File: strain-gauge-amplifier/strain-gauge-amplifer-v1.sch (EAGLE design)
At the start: 19 parts, among them IC2 INA125U, Q1 PMV45EN

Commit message: Cleaned up schematic, fixed a minor errors, ready for layout!
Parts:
- removed JP4: POT, SparkFun-Connectors:M025MM
- removed R2: 120, rcl_custom:R-US_0805-C-NOSILK
- removed R9: POT, SparkFun-Electromechanical:TRIMPOTTRIMPOT-5MM
- added C2, C4: 100n, rcl_custom:C-EU0805-C-NOSILK
- added C5: 1n, rcl_custom:C-EU0805-C-NOSILK
- added R2A: 100, rcl_custom:R-US_0805-C-NOSILK
- added R2B: 50ohm/20turn, SparkFun-Electromechanical:TRIMPOTTRIMPOT-5MM
- JP2: value OUT1 -> (none)
- JP3: value OUT2 -> (none)
- JP5: value RGAIN -> Rg
- R10: value 150 -> 1k
- R3: value 100 -> 120
- R4: value 100 -> 1k
- R6: value 0 -> NP (0)
- R7: value DNP/10k -> NP (10k)
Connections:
- removed net N$7: R3.1, R9.CCW
- net 2.5VREF: now also C2.1, C4.1, C5.1, JP1.2, R1.2; no longer JP4.2
- net GND: now also C2.2, C4.2, C5.2, R2B.CW, R3.1; no longer R2.1, R9.CW
- net N$1: now also R2A.1, R2B.WIPER; no longer JP1.2, JP4.1, R1.2
- net VIN+: now also R2A.2; no longer R3.2
- net VIN-: now also R3.2; no longer R2.2
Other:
- note added: "To DAQ"
- note removed: "50 OHM/20 TURNS"
- moved on the sheet: C1, C3, IC2, JP1, JP2, JP3, JP5, LED1, Q1, R1, R10, R3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

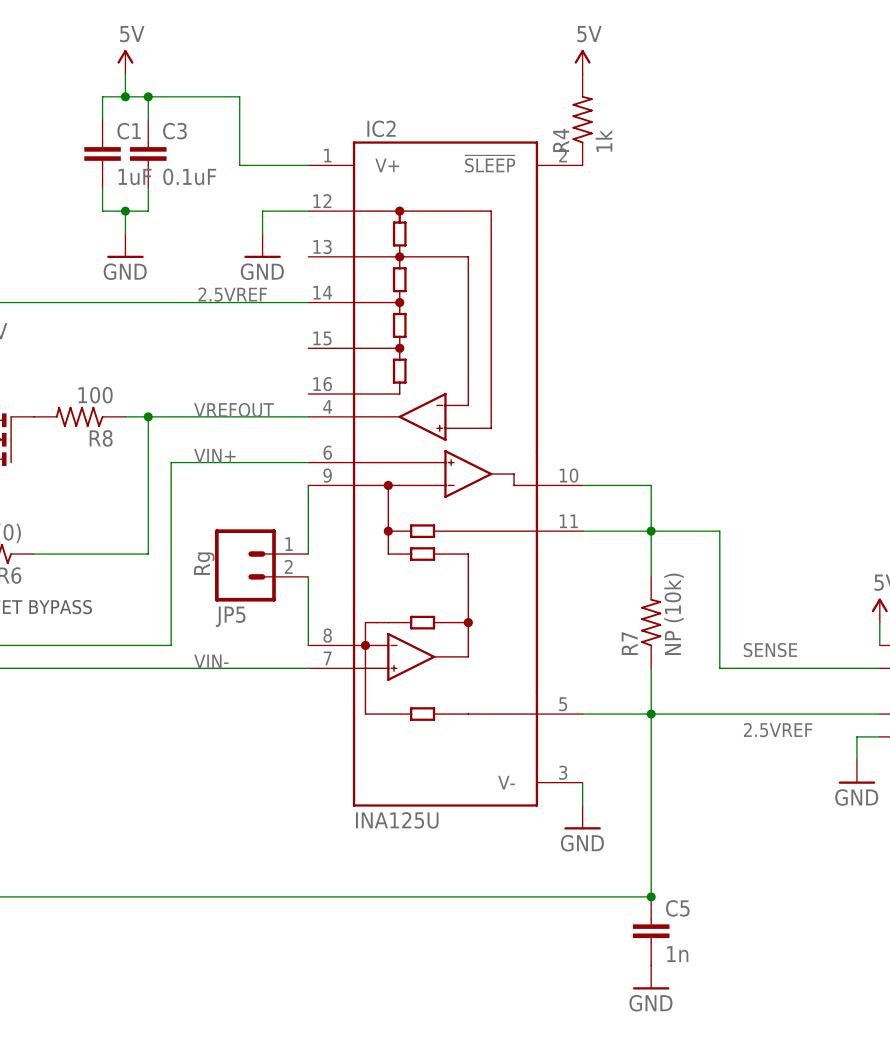
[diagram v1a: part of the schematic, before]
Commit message: Cleaned up and added BOM.
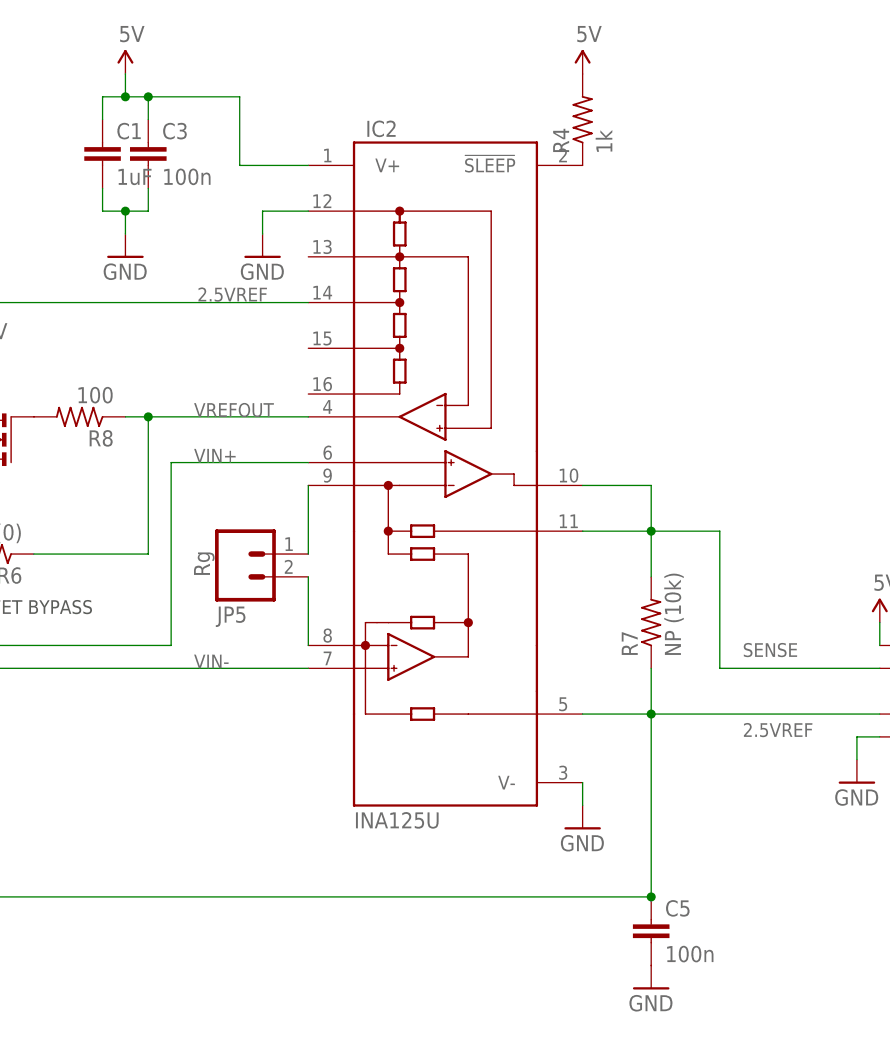
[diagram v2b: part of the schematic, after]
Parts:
- C3: value 0.1uF -> 100n
- C5: value 1n -> 100n
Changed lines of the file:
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@@
 <setting verticaltext="up"/>
 </settings>
-<grid distance="0.05" unitdist="inch" unit="inch" style="lines" multiple="2" display="yes" altdistance="0.01" altunitdist="inch" altunit="inch"/>
+<grid distance="0.1" unitdist="inch" unit="inch" style="lines" multiple="1" display="no" altdistance="0.01" altunitdist="inch" altunit="inch"/>
 <layers>
 <layer number="1" name="Top" color="4" fill="1" visible="no" active="no"/>
@@
 <parts>
 <part name="R4" library="rcl_custom" deviceset="R-US_" device="0805-C-NOSILK" value="1k"/>
-<part name="C3" library="rcl_custom" deviceset="C-EU" device="0805-C-NOSILK" value="0.1uF"/>
+<part name="C3" library="rcl_custom" deviceset="C-EU" device="0805-C-NOSILK" value="100n"/>
 <part name="U$3" library="SparkFun-Aesthetics" deviceset="5V" device=""/>
 <part name="JP1" library="SparkFun-Connectors" deviceset="M02" device="5MM" value="STRAIN"/>
@@
 <part name="C4" library="rcl_custom" deviceset="C-EU" device="0805-C-NOSILK" value="100n"/>
 <part name="GND8" library="SparkFun-Aesthetics" deviceset="GND" device=""/>
-<part name="C5" library="rcl_custom" deviceset="C-EU" device="0805-C-NOSILK" value="1n"/>
+<part name="C5" library="rcl_custom" deviceset="C-EU" device="0805-C-NOSILK" value="100n"/>
 <part name="GND9" library="SparkFun-Aesthetics" deviceset="GND" device=""/>
 </parts>
@@
 </sheet>
 </sheets>
+<errors>
+</errors>
 </schematic>
 </drawing>

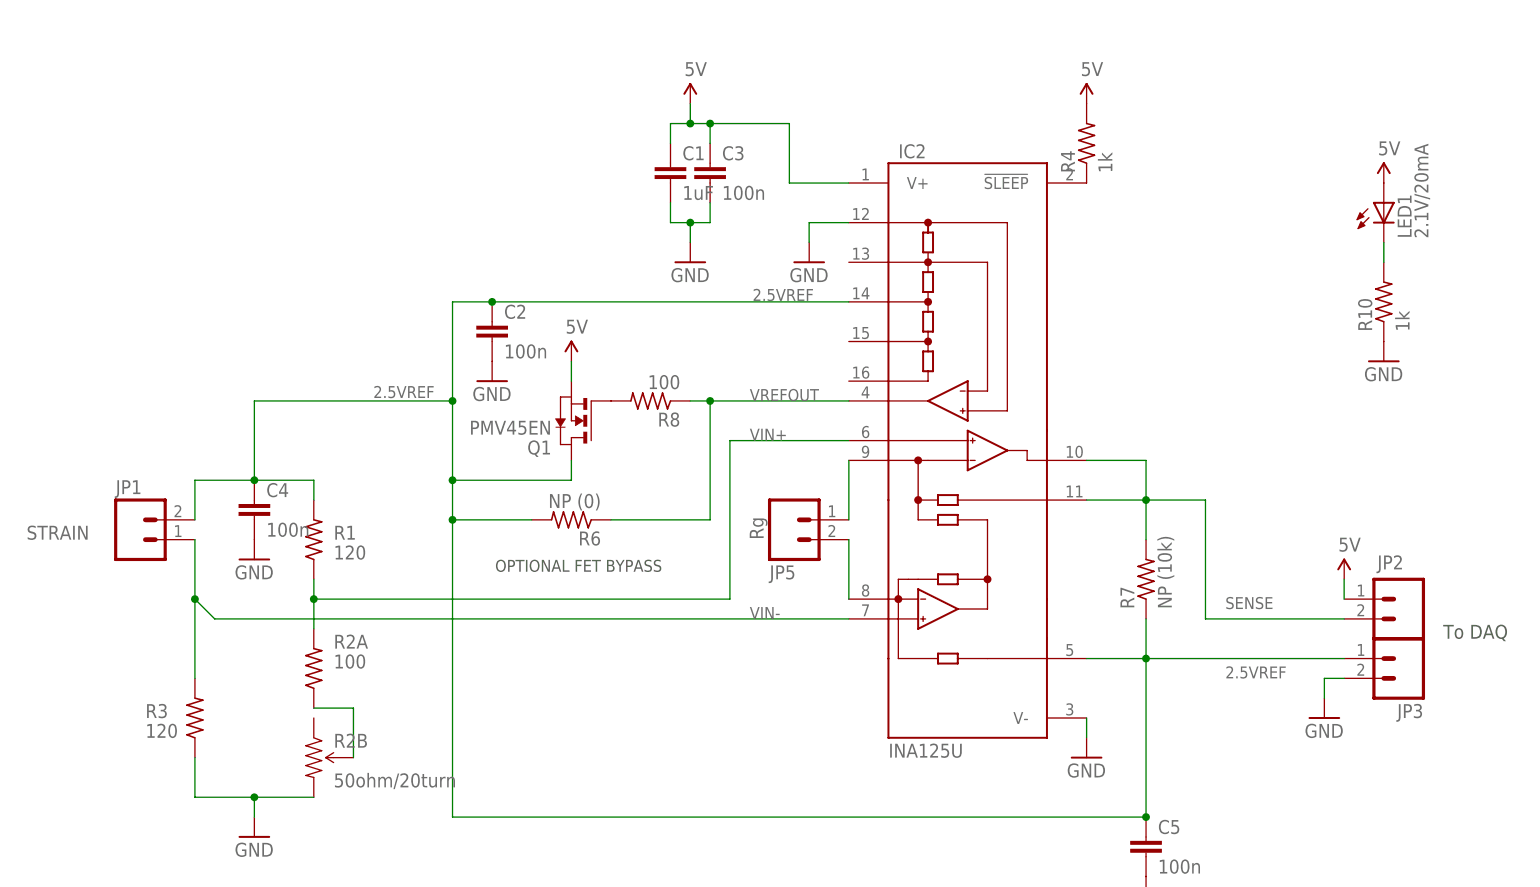
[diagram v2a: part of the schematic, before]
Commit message: Made board. Passes ERC, DRC.
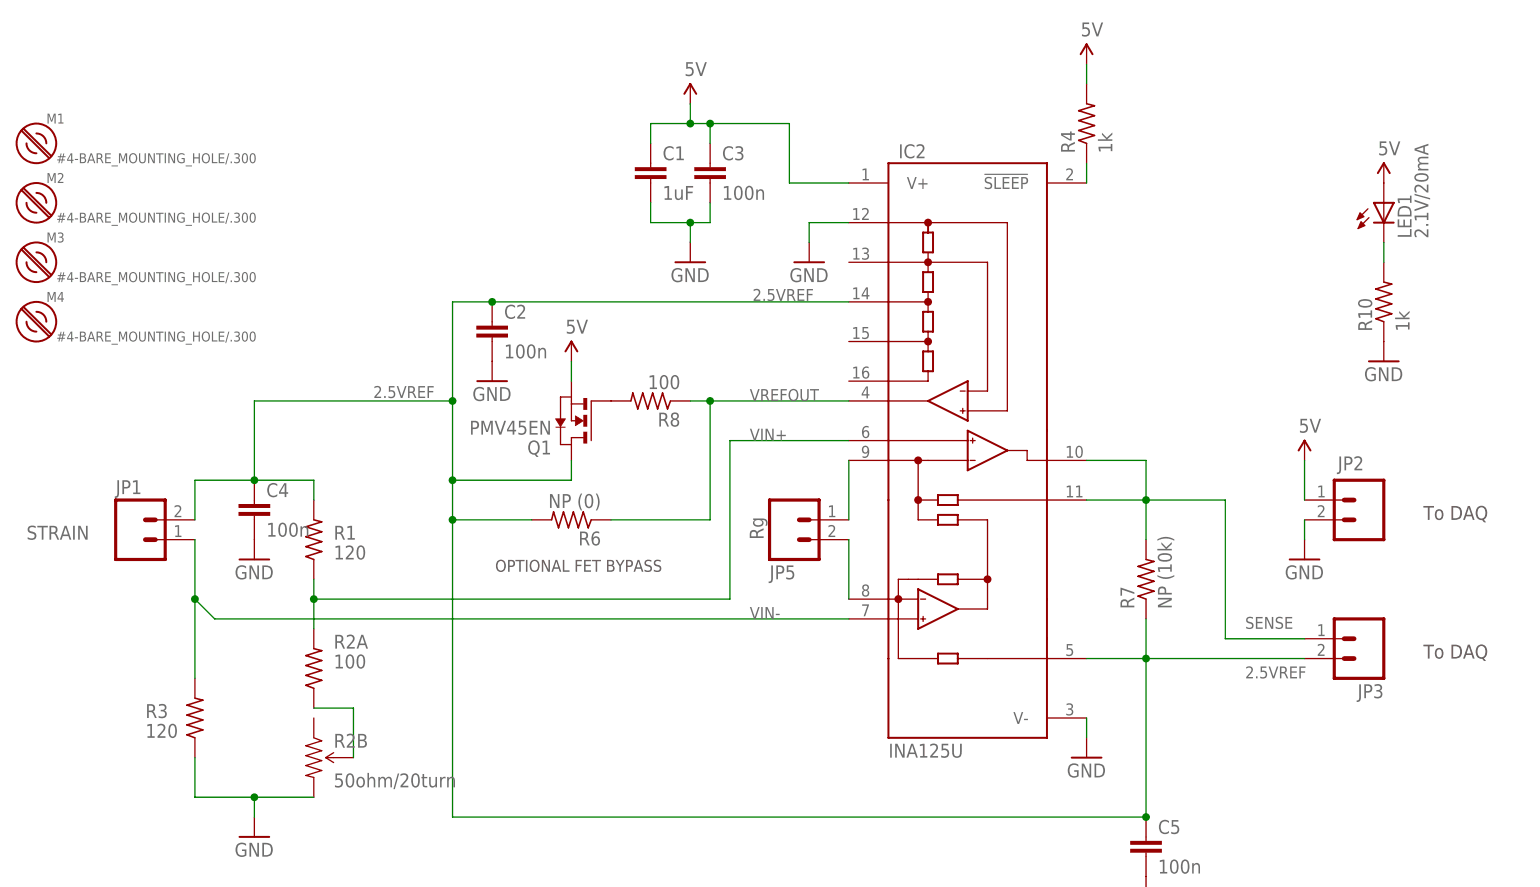
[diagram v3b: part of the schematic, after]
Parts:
- added M1, M2, M3, M4: #4-BARE_MOUNTING_HOLE/.300, mount:#4-BARE_MOUNTING_HOLE/.300
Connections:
- net 2.5VREF: now also JP3.2; no longer JP3.1
- net GND: now also JP2.2; no longer JP3.2
- net SENSE: now also JP3.1; no longer JP2.2
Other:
- moved on the sheet: C1, JP2, JP3, R4
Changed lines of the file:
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@@
 <?xml version="1.0" encoding="utf-8"?>
 <!DOCTYPE eagle SYSTEM "eagle.dtd">
-<eagle version="6.5.0">
+<eagle version="6.4">
 <drawing>
 <settings>
@@
 <setting verticaltext="up"/>
 </settings>
-<grid distance="0.1" unitdist="inch" unit="inch" style="lines" multiple="1" display="no" altdistance="0.01" altunitdist="inch" altunit="inch"/>
+<grid distance="0.1" unitdist="inch" unit="inch" style="dots" multiple="1" display="yes" altdistance="0.001" altunitdist="inch" altunit="inch"/>
 <layers>
 <layer number="1" name="Top" color="4" fill="1" visible="no" active="no"/>
@@
 <part name="C5" library="rcl_custom" deviceset="C-EU" device="0805-C-NOSILK" value="100n"/>
 <part name="GND9" library="SparkFun-Aesthetics" deviceset="GND" device=""/>
+<part name="M1" library="mount" deviceset="#4-BARE_MOUNTING_HOLE" device="/.300"/>
+<part name="M2" library="mount" deviceset="#4-BARE_MOUNTING_HOLE" device="/.300"/>
+<part name="M3" library="mount" deviceset="#4-BARE_MOUNTING_HOLE" device="/.300"/>
+<part name="M4" library="mount" deviceset="#4-BARE_MOUNTING_HOLE" device="/.300"/>
 </parts>
 <sheets>
@@
 <plain>
 <text x="94.361" y="107.6452" size="1.524" layer="97">OPTIONAL FET BYPASS</text>
-<text x="215.9" y="99.06" size="1.778" layer="97">To DAQ</text>
+<text x="213.36" y="96.52" size="1.778" layer="97">To DAQ</text>
+<text x="213.36" y="114.3" size="1.778" layer="97">To DAQ</text>
 </plain>
 <instances>
-<instance part="R4" gate="R" x="170.18" y="162.56" rot="R90"/>
+<instance part="R4" gate="R" x="170.18" y="165.1" rot="R90"/>
 <instance part="C3" gate="CE" x="121.92" y="160.02"/>
 <instance part="U$3" gate="G$1" x="119.38" y="167.64"/>
@@
 <attribute name="NAME" x="45.72" y="117.602" size="1.778" layer="95"/>
 </instance>
-<instance part="JP2" gate="G$1" x="210.82" y="104.14" smashed="yes" rot="R180">
-<attribute name="VALUE" x="213.36" y="109.22" size="1.778" layer="96" rot="R180"/>
-<attribute name="NAME" x="210.82" y="109.728" size="1.778" layer="95" rot="R180"/>
-</instance>
-<instance part="JP3" gate="G$1" x="210.82" y="96.52" rot="R180"/>
+<instance part="JP2" gate="G$1" x="205.74" y="116.84" smashed="yes" rot="R180">
+<attribute name="VALUE" x="208.28" y="121.92" size="1.778" layer="96" rot="R180"/>
+<attribute name="NAME" x="205.74" y="122.428" size="1.778" layer="95" rot="R180"/>
+</instance>
+<instance part="JP3" gate="G$1" x="205.74" y="99.06" rot="R180"/>
 <instance part="R3" gate="R" x="55.88" y="88.9" smashed="yes" rot="R90">
 <attribute name="NAME" x="49.53" y="88.9" size="1.778" layer="95"/>
@@
 </instance>
 <instance part="GND2" gate="1" x="119.38" y="147.32"/>
-<instance part="U$1" gate="G$1" x="170.18" y="167.64"/>
-<instance part="GND1" gate="1" x="200.66" y="88.9"/>
+<instance part="U$1" gate="G$1" x="170.18" y="172.72"/>
+<instance part="GND1" gate="1" x="198.12" y="109.22"/>
 <instance part="R7" gate="R" x="177.8" y="106.68" rot="R90"/>
 <instance part="Q1" gate="G$1" x="104.14" y="127" rot="R180"/>
@@
 <instance part="R10" gate="R" x="208.28" y="142.24" rot="R90"/>
 <instance part="GND3" gate="1" x="208.28" y="134.62"/>
-<instance part="C1" gate="CE" x="116.84" y="160.02"/>
+<instance part="C1" gate="CE" x="114.3" y="160.02"/>
 <instance part="JP5" gate="G$1" x="132.08" y="114.3" smashed="yes" rot="MR180">
 <attribute name="VALUE" x="127" y="111.76" size="1.778" layer="96" rot="MR90"/>
@@
 <instance part="FRAME1" gate="G$1" x="0" y="0"/>
 <instance part="FRAME1" gate="G$2" x="172.72" y="0"/>
-<instance part="U$4" gate="G$1" x="203.2" y="106.68"/>
+<instance part="U$4" gate="G$1" x="198.12" y="121.92"/>
 <instance part="GND4" gate="1" x="170.18" y="83.82"/>
 <instance part="U$5" gate="G$1" x="208.28" y="157.48"/>
@@
 <instance part="C5" gate="CE" x="177.8" y="73.66"/>
 <instance part="GND9" gate="1" x="177.8" y="66.04"/>
+<instance part="M1" gate="MT" x="35.56" y="162.56"/>
+<instance part="M2" gate="MT" x="35.56" y="154.94"/>
+<instance part="M3" gate="MT" x="35.56" y="147.32"/>
+<instance part="M4" gate="MT" x="35.56" y="139.7"/>
 </instances>
 <busses>
@@
 <wire x1="121.92" y1="152.4" x2="121.92" y2="154.94" width="0.1524" layer="91"/>
 <pinref part="C1" gate="CE" pin="2"/>
-<wire x1="116.84" y1="154.94" x2="116.84" y2="152.4" width="0.1524" layer="91"/>
-<wire x1="116.84" y1="152.4" x2="119.38" y2="152.4" width="0.1524" layer="91"/>
+<wire x1="114.3" y1="154.94" x2="114.3" y2="152.4" width="0.1524" layer="91"/>
+<wire x1="114.3" y1="152.4" x2="119.38" y2="152.4" width="0.1524" layer="91"/>
 <wire x1="119.38" y1="152.4" x2="121.92" y2="152.4" width="0.1524" layer="91"/>
 <wire x1="119.38" y1="149.86" x2="119.38" y2="152.4" width="0.1524" layer="91"/>
@@
 <pinref part="GND4" gate="1" pin="GND"/>
 <wire x1="170.18" y1="86.36" x2="170.18" y2="88.9" width="0.1524" layer="91"/>
-</segment>
-<segment>
-<pinref part="GND1" gate="1" pin="GND"/>
-<pinref part="JP3" gate="G$1" pin="2"/>
-<wire x1="203.2" y1="93.98" x2="200.66" y2="93.98" width="0.1524" layer="91"/>
-<wire x1="200.66" y1="93.98" x2="200.66" y2="91.44" width="0.1524" layer="91"/>
 </segment>
 <segment>
@@
 <pinref part="GND9" gate="1" pin="GND"/>
 </segment>
+<segment>
+<pinref part="JP2" gate="G$1" pin="2"/>
+<pinref part="GND1" gate="1" pin="GND"/>
+<wire x1="198.12" y1="111.76" x2="198.12" y2="114.3" width="0.1524" layer="91"/>
+</segment>
 </net>
 <net name="N$3" class="0">
@@
 <wire x1="177.8" y1="116.84" x2="170.18" y2="116.84" width="0.1524" layer="91"/>
 <junction x="177.8" y="116.84"/>
-<wire x1="177.8" y1="116.84" x2="185.42" y2="116.84" width="0.1524" layer="91"/>
-<wire x1="185.42" y1="116.84" x2="185.42" y2="101.6" width="0.1524" layer="91"/>
-<wire x1="185.42" y1="101.6" x2="203.2" y2="101.6" width="0.1524" layer="91"/>
-<label x="187.96" y="102.87" size="1.524" layer="95"/>
+<wire x1="177.8" y1="116.84" x2="187.96" y2="116.84" width="0.1524" layer="91"/>
+<wire x1="187.96" y1="116.84" x2="187.96" y2="99.06" width="0.1524" layer="91"/>
+<wire x1="187.96" y1="99.06" x2="198.12" y2="99.06" width="0.1524" layer="91"/>
+<label x="190.5" y="100.33" size="1.524" layer="95"/>
 <pinref part="R7" gate="R" pin="2"/>
 <wire x1="177.8" y1="116.84" x2="177.8" y2="111.76" width="0.1524" layer="91"/>
-<pinref part="JP2" gate="G$1" pin="2"/>
+<pinref part="JP3" gate="G$1" pin="1"/>
 </segment>
 </net>
@@
 <wire x1="121.92" y1="165.1" x2="119.38" y2="165.1" width="0.1524" layer="91"/>
 <pinref part="C1" gate="CE" pin="1"/>
-<wire x1="119.38" y1="165.1" x2="116.84" y2="165.1" width="0.1524" layer="91"/>
-<wire x1="116.84" y1="165.1" x2="116.84" y2="162.56" width="0.1524" layer="91"/>
+<wire x1="119.38" y1="165.1" x2="114.3" y2="165.1" width="0.1524" layer="91"/>
+<wire x1="114.3" y1="165.1" x2="114.3" y2="162.56" width="0.1524" layer="91"/>
 <wire x1="119.38" y1="167.64" x2="119.38" y2="165.1" width="0.1524" layer="91"/>
 <junction x="119.38" y="165.1"/>
@@
 <pinref part="U$4" gate="G$1" pin="5V"/>
 <pinref part="JP2" gate="G$1" pin="1"/>
-<wire x1="203.2" y1="104.14" x2="203.2" y2="106.68" width="0.1524" layer="91"/>
+<wire x1="198.12" y1="116.84" x2="198.12" y2="121.92" width="0.1524" layer="91"/>
 </segment>
 <segment>
 <pinref part="R4" gate="R" pin="2"/>
 <pinref part="U$1" gate="G$1" pin="5V"/>
+<wire x1="170.18" y1="172.72" x2="170.18" y2="170.18" width="0.1524" layer="91"/>
 </segment>
 <segment>
@@
 <pinref part="IC2" gate="G$1" pin="!SLEEP"/>
 <pinref part="R4" gate="R" pin="1"/>
+<wire x1="170.18" y1="160.02" x2="170.18" y2="157.48" width="0.1524" layer="91"/>
 </segment>
 </net>
@@
 <junction x="177.8" y="96.52"/>
 <wire x1="177.8" y1="96.52" x2="177.8" y2="101.6" width="0.1524" layer="91"/>
-<label x="187.96" y="93.98" size="1.524" layer="95"/>
+<label x="190.5" y="93.98" size="1.524" layer="95"/>
 <wire x1="88.9" y1="76.2" x2="177.8" y2="76.2" width="0.1524" layer="91"/>
 <wire x1="177.8" y1="76.2" x2="177.8" y2="96.52" width="0.1524" layer="91"/>
-<wire x1="177.8" y1="96.52" x2="203.2" y2="96.52" width="0.1524" layer="91"/>
-<pinref part="JP3" gate="G$1" pin="1"/>
 <junction x="88.9" y="114.3"/>
 <label x="127.3556" y="142.367" size="1.524" layer="95"/>
@@
 <pinref part="C5" gate="CE" pin="1"/>
 <junction x="177.8" y="76.2"/>
-</segment>
-</net>
+<pinref part="JP3" gate="G$1" pin="2"/>
+<wire x1="177.8" y1="96.52" x2="198.12" y2="96.52" width="0.1524" layer="91"/>
+</segment>
+</net>
